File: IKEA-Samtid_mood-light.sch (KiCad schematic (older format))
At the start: 16 parts, among them IC1 ATMEGA168PA-M, P1 FTDI, P2 POWER, P3.1 B-to-B-1A, P3.2 B-to-B-1B, P4.1 B-to-B-2A, P4.2 B-to-B-2B, SW1 ENTER, SW2 MODE, X1 CSTCE16M0V53-R0

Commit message: Might be the first prototype.
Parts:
- added Q1, Q2: BSS138, SOT-23, symbol BSS138
- added Rp1, Rp2: 4k7, symbol R
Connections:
- net +5V: now also Q2.1 (G), Rp1.1
- net GND.A: now also P2.1 (P1); no longer P2.3 (P3)
- net TXO/LEDs: now also Q2.2 (S), Rp1.2
- net VCC.A: now also Q1.1 (G), Rp2.1
- net at F1.1, F2.1, P2.2 (P2): now also P2.3 (P3); no longer P2.1 (P1)
- new net: Q1.3 (D), Q2.3 (D)
- new net WS2812B-LEDs-1/A_IN: Q1.2 (S), Rp2.2
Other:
- note added: "(2) Signal isolation if either \npower source is absent"
- note added: "(2) We don't want any power bleeding through input clamping diodes when just the programmer is connected and the main power supply if off."
- note removed: "(2) ---"
- moved on the sheet: DS1, DS2, F1, F2, P2

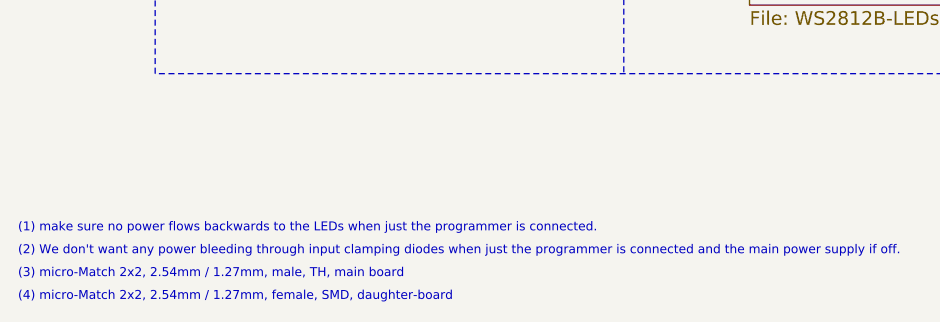
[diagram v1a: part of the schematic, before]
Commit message: Added part numbers for the micro-Match connectors.
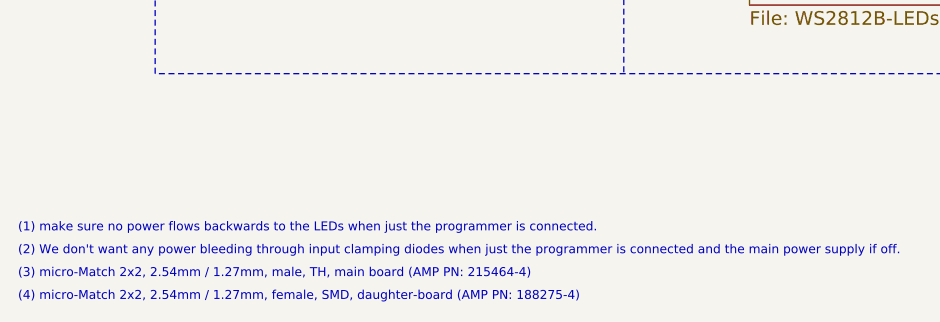
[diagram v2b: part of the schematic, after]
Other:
- note added: "(3) micro-Match 2x2, 2.54mm / 1.27mm, male, TH, main board (AMP PN: 215464-4)"
- note added: "(4) micro-Match 2x2, 2.54mm / 1.27mm, female, SMD, daughter-board (AMP PN: 188275-4)"
- note removed: "(3) micro-Match 2x2, 2.54mm / 1.27mm, male, TH, main board"
- note removed: "(4) micro-Match 2x2, 2.54mm / 1.27mm, female, SMD, daughter-board"
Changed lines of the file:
@@
 Sheet 1 3
 Title "IKEA-Samtid_mood-light"
-Date "13 Jul 2014"
+Date "14 Jul 2014"
 Rev "0.17"
 Comp "2014 - blog.spitzenpfeil.org"
@@
 $EndComp
 Text Notes 550  7600 0    39   ~ 0
-(3) micro-Match 2x2, 2.54mm / 1.27mm, male, TH, main board
+(3) micro-Match 2x2, 2.54mm / 1.27mm, male, TH, main board (AMP PN: 215464-4)
 Text Notes 550  7700 0    39   ~ 0
-(4) micro-Match 2x2, 2.54mm / 1.27mm, female, SMD, daughter-board
+(4) micro-Match 2x2, 2.54mm / 1.27mm, female, SMD, daughter-board (AMP PN: 188275-4)
 Text Notes 8550 1400 0    39   ~ 0
 (3)

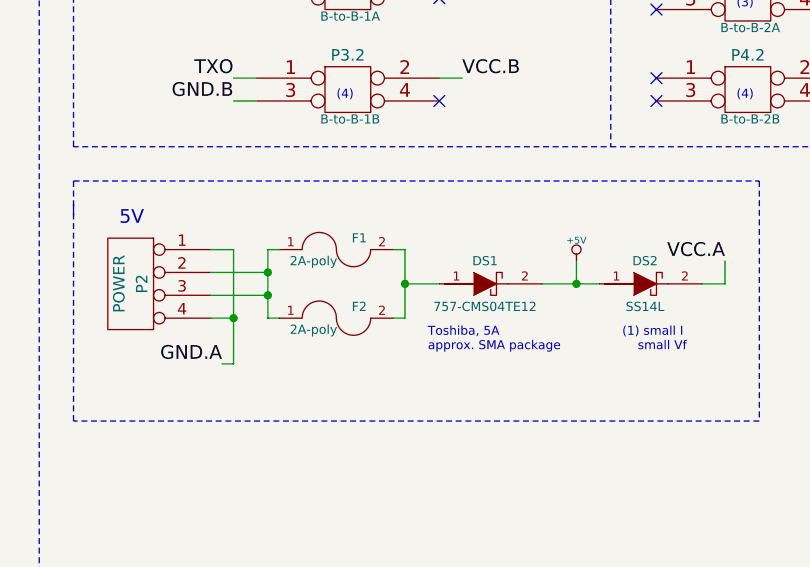
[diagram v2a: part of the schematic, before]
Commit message: Changed main Schottky to SK84B (beefier, bigger package, SMC).
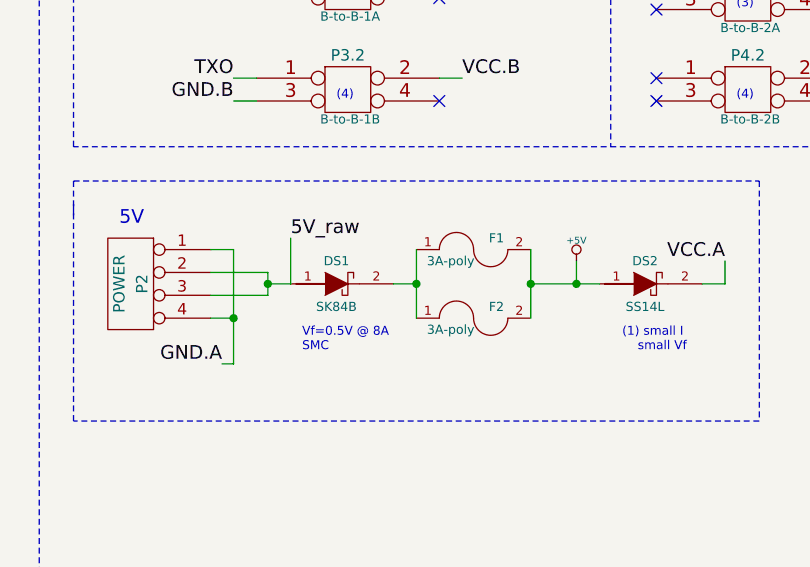
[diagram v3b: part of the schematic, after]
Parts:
- DS1: value 757-CMS04TE12 -> SK84B
- F1, F2: value 2A-poly -> 3A-poly
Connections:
- net +5V: now also F1.2, F2.2; no longer DS1.2 (C)
- net at F1.1, F2.1: now also DS1.2 (C); no longer P2.2 (P2), P2.3 (P3)
- new net 5V_raw: DS1.1 (A), P2.2 (P2), P2.3 (P3)
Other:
- note added: "Vf=0.5V @ 8A\nSMC"
- note removed: "Toshiba, 5A\napprox. SMA package"
- moved on the sheet: DS1, F1, F2
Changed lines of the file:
@@
 Sheet 1 3
 Title "IKEA-Samtid_mood-light"
-Date "14 Jul 2014"
-Rev "0.17"
+Date "15 Jul 2014"
+Rev "0.19"
 Comp "2014 - blog.spitzenpfeil.org"
 Comment1 ""
@@
 L FUSE F1
 U 1 1 53C3478B
-P 8550 2500
-F 0 "F1" H 8650 2550 40  0000 C CNN
-F 1 "2A-poly" H 8450 2450 40  0000 C CNN
-F 2 "" H 8550 2500 60  0000 C CNN
-F 3 "" H 8550 2500 60  0000 C CNN
-	1    8550 2500
+P 9150 2500
+F 0 "F1" H 9250 2550 40  0000 C CNN
+F 1 "3A-poly" H 9050 2450 40  0000 C CNN
+F 2 "" H 9150 2500 60  0000 C CNN
+F 3 "" H 9150 2500 60  0000 C CNN
+	1    9150 2500
 	1    0    0    -1
 $EndComp
@@
 L FUSE F2
 U 1 1 53C34893
-P 8550 2800
-F 0 "F2" H 8650 2850 40  0000 C CNN
-F 1 "2A-poly" H 8450 2750 40  0000 C CNN
-F 2 "" H 8550 2800 60  0000 C CNN
-F 3 "" H 8550 2800 60  0000 C CNN
-	1    8550 2800
+P 9150 2800
+F 0 "F2" H 9250 2850 40  0000 C CNN
+F 1 "3A-poly" H 9050 2750 40  0000 C CNN
+F 2 "" H 9150 2800 60  0000 C CNN
+F 3 "" H 9150 2800 60  0000 C CNN
+	1    9150 2800
 	1    0    0    -1
 $EndComp
@@
 L DIODESCH DS1
 U 1 1 53C35916
-P 9200 2650
-F 0 "DS1" H 9200 2750 40  0000 C CNN
-F 1 "757-CMS04TE12" H 9200 2550 40  0000 C CNN
-F 2 "" H 9200 2650 60  0000 C CNN
-F 3 "" H 9200 2650 60  0000 C CNN
-	1    9200 2650
+P 8550 2650
+F 0 "DS1" H 8550 2750 40  0000 C CNN
+F 1 "SK84B" H 8550 2550 40  0000 C CNN
+F 2 "" H 8550 2650 60  0000 C CNN
+F 3 "" H 8550 2650 60  0000 C CNN
+	1    8550 2650
 	1    0    0    -1
 $EndComp
@@
 Text Label 6850 1550 3    60   ~ 0
 XTAL2
-Text Notes 8950 2950 0    39   ~ 0
-Toshiba, 5A\napprox. SMA package
 $Comp
 L ATMEGA168PA-M IC1
@@
 	7200 900  1150 900
 Wire Wire Line
-	8800 2500 8850 2500
-Wire Wire Line
-	8850 2500 8850 2800
-Wire Wire Line
-	8300 2500 8250 2500
-Wire Wire Line
-	8850 2800 8800 2800
-Wire Wire Line
-	8250 2800 8300 2800
-Wire Wire Line
-	8850 2650 9000 2650
-Connection ~ 8850 2650
-Wire Wire Line
-	9450 2650 9700 2650
+	9400 2650 9700 2650
 Wire Notes Line
 	7400 2300 7400 3250
@@
 	8100 2800 8000 2800
 Wire Wire Line
-	8250 2500 8250 2800
-Wire Wire Line
-	8000 2700 8250 2700
-Connection ~ 8250 2700
+	8250 2700 8000 2700
 Wire Wire Line
 	8000 2600 8250 2600
-Connection ~ 8250 2600
 Wire Notes Line
 	7400 2200 10400 2200
@@
 Wire Wire Line
 	8100 3000 8050 3000
+Wire Wire Line
+	8250 2650 8350 2650
+Connection ~ 8250 2650
+Text Notes 8400 2950 0    39   ~ 0
+Vf=0.5V @ 8A\nSMC
+Wire Wire Line
+	9400 2500 9400 2800
+Connection ~ 9400 2650
+Wire Wire Line
+	8900 2500 8900 2800
+Wire Wire Line
+	8800 2650 8900 2650
+Connection ~ 8900 2650
+Text Label 8350 2450 0    60   ~ 0
+5V_raw
+Wire Wire Line
+	8250 2600 8250 2700
+Wire Wire Line
+	8350 2650 8350 2450
 $EndSCHEMATC

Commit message: Swapped male / female micro-MaTch connectors. Adjusted spacer board.
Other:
- note added: "(3) micro-Match 2x2, 2.54mm / 1.27mm, female, SMD, main-board (AMP PN: 188275-4)"
- note added: "(4) micro-Match 2x2, 2.54mm / 1.27mm, male, TH, daughter-board (AMP PN: 215464-4)"
- note removed: "(3) micro-Match 2x2, 2.54mm / 1.27mm, male, TH, main board (AMP PN: 215464-4)"
- note removed: "(4) micro-Match 2x2, 2.54mm / 1.27mm, female, SMD, daughter-board (AMP PN: 188275-4)"
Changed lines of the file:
@@
 Sheet 1 3
 Title "IKEA-Samtid_mood-light"
-Date "15 Jul 2014"
-Rev "0.19"
+Date "24 Jul 2014"
+Rev "0.20"
 Comp "2014 - blog.spitzenpfeil.org"
 Comment1 ""
@@
 	1    0    0    -1
 $EndComp
+Text Notes 550  7700 0    39   ~ 0
+(4) micro-Match 2x2, 2.54mm / 1.27mm, male, TH, daughter-board (AMP PN: 215464-4)
 Text Notes 550  7600 0    39   ~ 0
-(3) micro-Match 2x2, 2.54mm / 1.27mm, male, TH, main board (AMP PN: 215464-4)
-Text Notes 550  7700 0    39   ~ 0
-(4) micro-Match 2x2, 2.54mm / 1.27mm, female, SMD, daughter-board (AMP PN: 188275-4)
+(3) micro-Match 2x2, 2.54mm / 1.27mm, female, SMD, main-board (AMP PN: 188275-4)
 Text Notes 8550 1400 0    39   ~ 0
 (3)

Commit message: Sanity checking + tweaks here and there.
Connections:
- net GND.A: now also P3.1.4
- net GND.B: now also P3.2.4
- no-connect marks 29 -> 27
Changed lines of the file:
@@
 Title "IKEA-Samtid_mood-light"
 Date "24 Jul 2014"
-Rev "0.20"
+Rev "0.21"
 Comp "2014 - blog.spitzenpfeil.org"
 Comment1 ""
@@
 Text Notes 9950 1050 0    60   ~ 0
 (just mechanical)
-NoConn ~ 9000 1850
-NoConn ~ 9000 1400
 Text Label 10250 2550 2    60   ~ 0
 VCC.A
@@
 Wire Wire Line
 	8350 2650 8350 2450
+Text Label 9100 1400 0    60   ~ 0
+GND.A
+Wire Wire Line
+	9000 1400 9100 1400
+Text Label 9100 1850 0    60   ~ 0
+GND.B
+Wire Wire Line
+	9000 1850 9100 1850
 $EndSCHEMATC

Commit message: Added a status LED.
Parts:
- added D65: LED, symbol LED
- added R1: 1k, symbol R
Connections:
- net GND.B: now also R1.2
- net SCK: now also D65.1 (A)
- new net: D65.2 (K), R1.1
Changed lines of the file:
@@
 Sheet 1 3
 Title "IKEA-Samtid_mood-light"
-Date "24 Jul 2014"
-Rev "0.21"
+Date "25 Jul 2014"
+Rev "0.22"
 Comp "2014 - blog.spitzenpfeil.org"
 Comment1 ""
@@
 L PWR_FLAG #FLG03
 U 1 1 53BF0941
-P 6500 3800
-F 0 "#FLG03" H 6500 3895 30  0001 C CNN
-F 1 "PWR_FLAG" H 6500 3980 30  0000 C CNN
-F 2 "" H 6500 3800 60  0000 C CNN
-F 3 "" H 6500 3800 60  0000 C CNN
-	1    6500 3800
+P 5850 3800
+F 0 "#FLG03" H 5850 3895 30  0001 C CNN
+F 1 "PWR_FLAG" H 5850 3980 30  0000 C CNN
+F 2 "" H 5850 3800 60  0000 C CNN
+F 3 "" H 5850 3800 60  0000 C CNN
+	1    5850 3800
 	1    0    0    -1
 $EndComp
@@
 L PWR_FLAG #FLG05
 U 1 1 53C2B991
-P 6950 3800
-F 0 "#FLG05" H 6950 3895 30  0001 C CNN
-F 1 "PWR_FLAG" H 6950 3980 30  0000 C CNN
-F 2 "" H 6950 3800 60  0000 C CNN
-F 3 "" H 6950 3800 60  0000 C CNN
-	1    6950 3800
+P 6300 3800
+F 0 "#FLG05" H 6300 3895 30  0001 C CNN
+F 1 "PWR_FLAG" H 6300 3980 30  0000 C CNN
+F 2 "" H 6300 3800 60  0000 C CNN
+F 3 "" H 6300 3800 60  0000 C CNN
+	1    6300 3800
 	1    0    0    -1
 $EndComp
@@
 Text Label 2400 3550 0    60   ~ 0
 VCC.B
-Text Label 6950 4000 2    60   ~ 0
+Text Label 6300 4000 2    60   ~ 0
 VCC.B
 Text Label 1800 2300 2    60   ~ 0
@@
 Text Label 6550 2000 0    60   ~ 0
 GND.B
-Text Label 6500 4000 2    60   ~ 0
+Text Label 5850 4000 2    60   ~ 0
 GND.B
 Text Label 8100 1850 2    60   ~ 0
@@
 	10000 6050 10000 6150
 Wire Wire Line
-	6500 3800 6500 4000
+	5850 3800 5850 4000
 Wire Wire Line
 	3300 5000 3750 5000
@@
 	5950 2800 6000 2800
 Wire Wire Line
-	6950 3800 6950 4000
+	6300 3800 6300 4000
 Wire Notes Line
 	7250 900  7100 900
@@
 Wire Wire Line
 	9000 1850 9100 1850
+$Comp
+L LED D65
+U 1 1 53D25751
+P 6700 3250
+F 0 "D65" H 6700 3350 50  0000 C CNN
+F 1 "LED" H 6700 3150 50  0000 C CNN
+F 2 "" H 6700 3250 60  0000 C CNN
+F 3 "" H 6700 3250 60  0000 C CNN
+	1    6700 3250
+	1    0    0    -1
+$EndComp
+$Comp
+L R R1
+U 1 1 53D25DCF
+P 6950 3550
+F 0 "R1" V 7030 3550 40  0000 C CNN
+F 1 "1k" V 6957 3551 40  0000 C CNN
+F 2 "" V 6880 3550 30  0000 C CNN
+F 3 "" H 6950 3550 30  0000 C CNN
+	1    6950 3550
+	1    0    0    -1
+$EndComp
+Wire Wire Line
+	6950 3250 6950 3300
+Text Label 6950 4000 2    60   ~ 0
+GND.B
+Wire Wire Line
+	6950 3800 6950 4000
+Text Label 6450 3250 2    60   ~ 0
+SCK
+Wire Wire Line
+	6450 3250 6500 3250
+Wire Wire Line
+	6900 3250 6950 3250
 $EndSCHEMATC

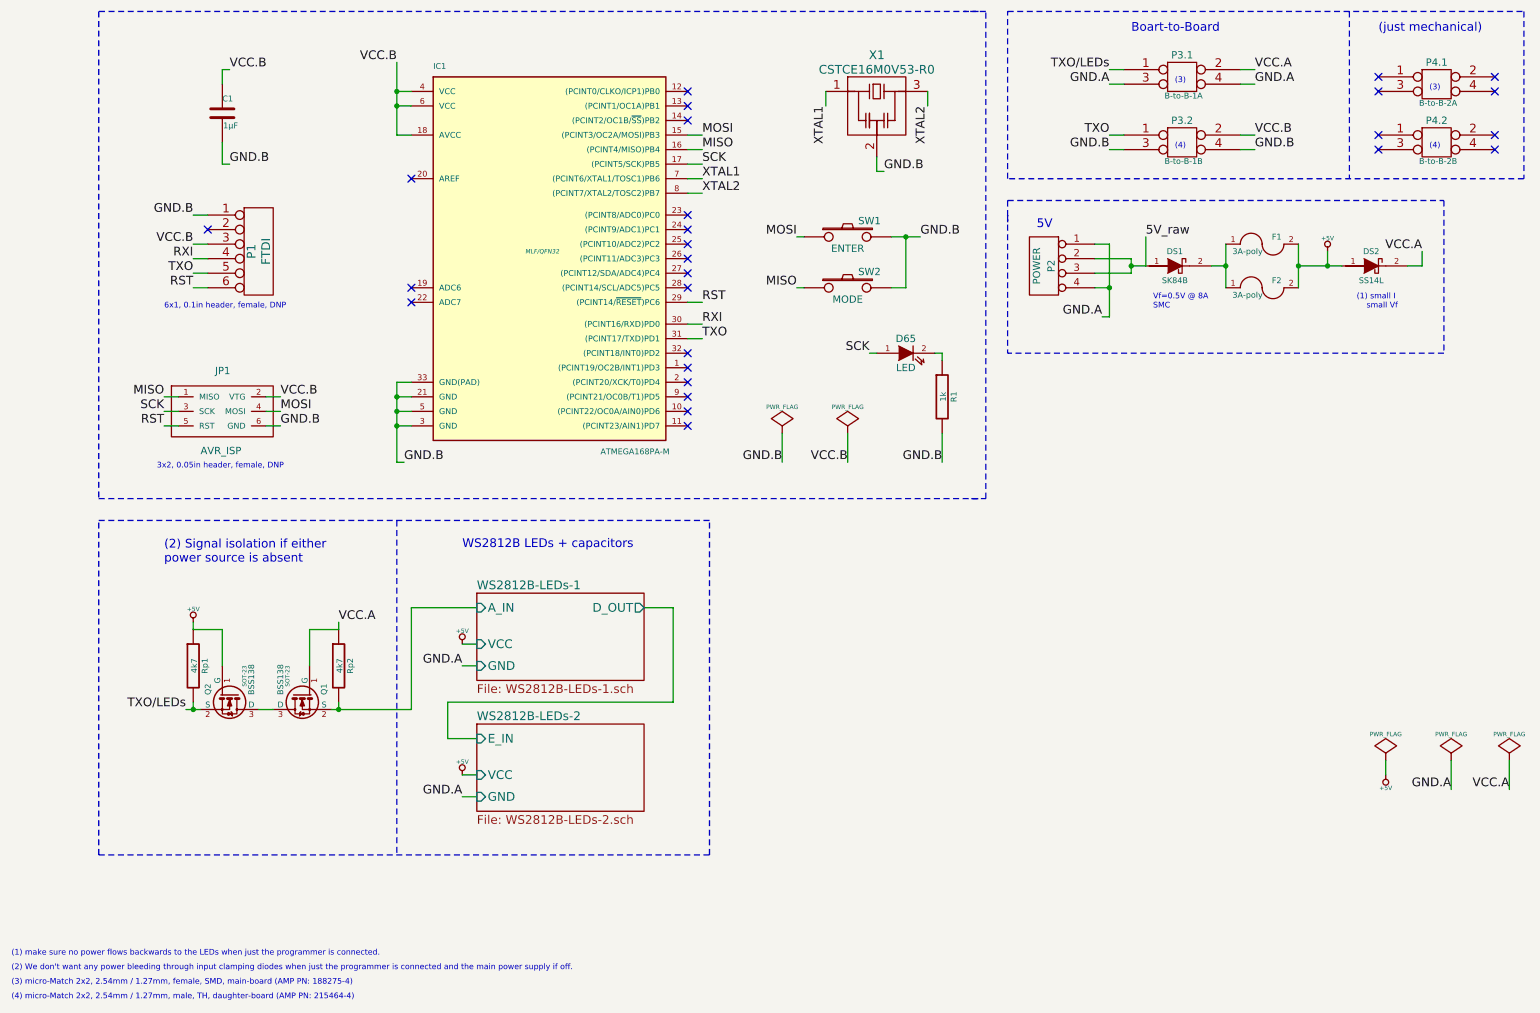
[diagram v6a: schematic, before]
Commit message: Had the pull-up voltages reversed on the MOSFET isolator.
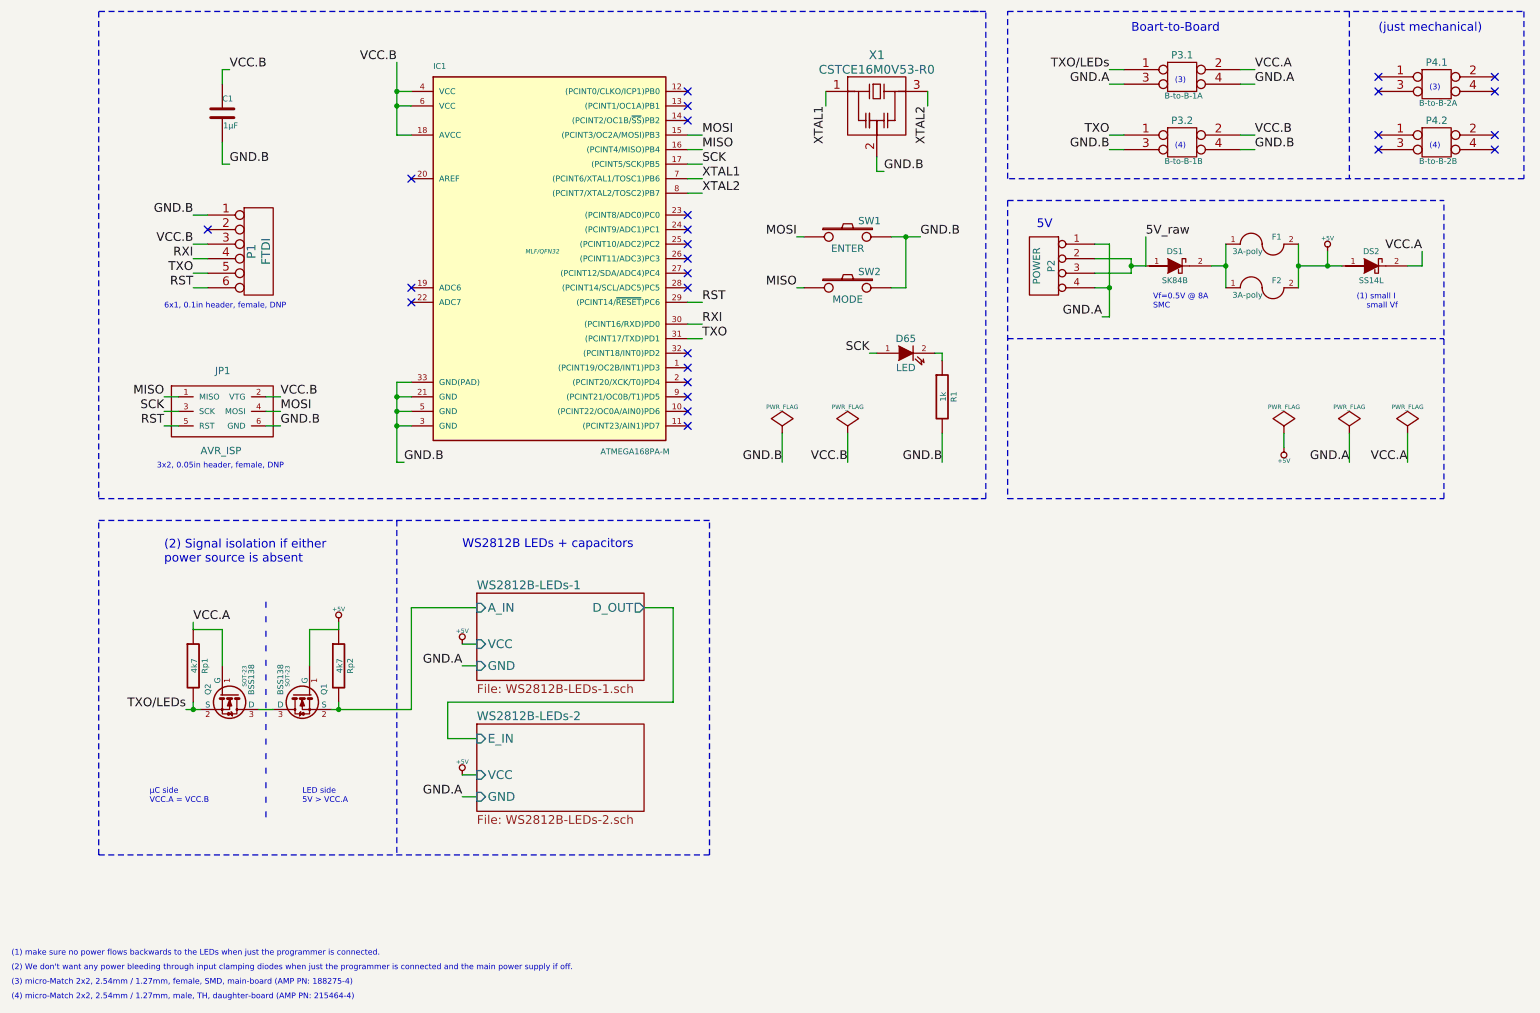
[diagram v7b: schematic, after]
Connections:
- net +5V: now also Q1.1 (G), Rp2.1; no longer Q2.1 (G), Rp1.1
- net VCC.A: now also Q2.1 (G), Rp1.1; no longer Q1.1 (G), Rp2.1
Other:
- note added: "LED side\n5V > VCC.A"
- note added: "µC side\nVCC.A = VCC.B"

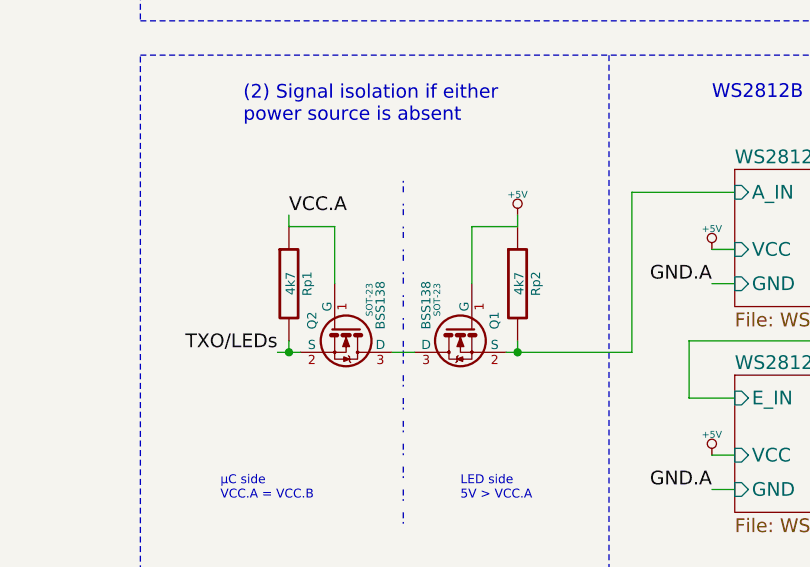
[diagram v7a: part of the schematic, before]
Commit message: Changed pull-up resistors to 1.5k. Roughly following: (VCC-0.4)/0.003
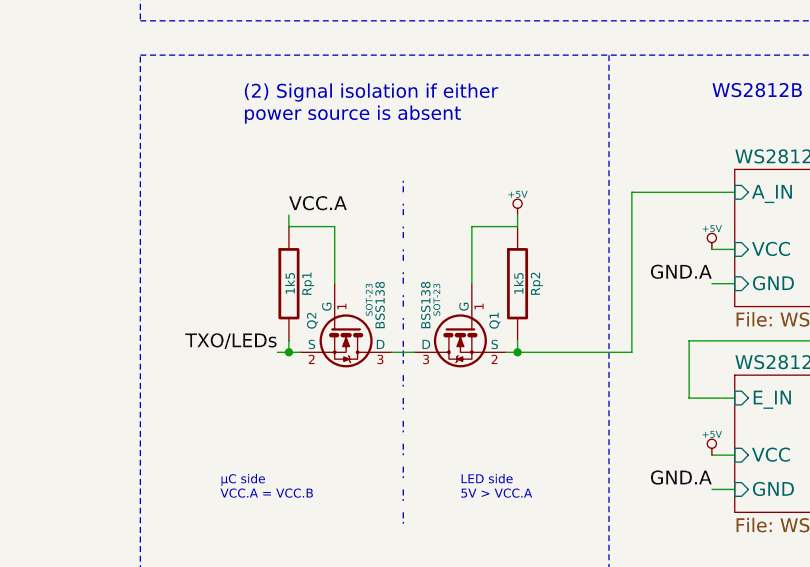
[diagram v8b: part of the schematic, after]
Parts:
- Rp1, Rp2: value 4k7 -> 1k5
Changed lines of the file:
@@
 Sheet 1 3
 Title "IKEA-Samtid_mood-light"
-Date "25 Jul 2014"
-Rev "0.23"
+Date "26 Jul 2014"
+Rev "0.24"
 Comp "2014 - blog.spitzenpfeil.org"
 Comment1 ""
@@
 P 1800 5400
 F 0 "Rp1" V 1880 5400 40  0000 C CNN
-F 1 "4k7" V 1807 5401 40  0000 C CNN
+F 1 "1k5" V 1807 5401 40  0000 C CNN
 F 2 "" V 1730 5400 30  0000 C CNN
 F 3 "" H 1800 5400 30  0000 C CNN
@@
 P 2800 5400
 F 0 "Rp2" V 2880 5400 40  0000 C CNN
-F 1 "4k7" V 2807 5401 40  0000 C CNN
+F 1 "1k5" V 2807 5401 40  0000 C CNN
 F 2 "" V 2730 5400 30  0000 C CNN
 F 3 "" H 2800 5400 30  0000 C CNN
